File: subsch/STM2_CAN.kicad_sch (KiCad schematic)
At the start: 17 parts

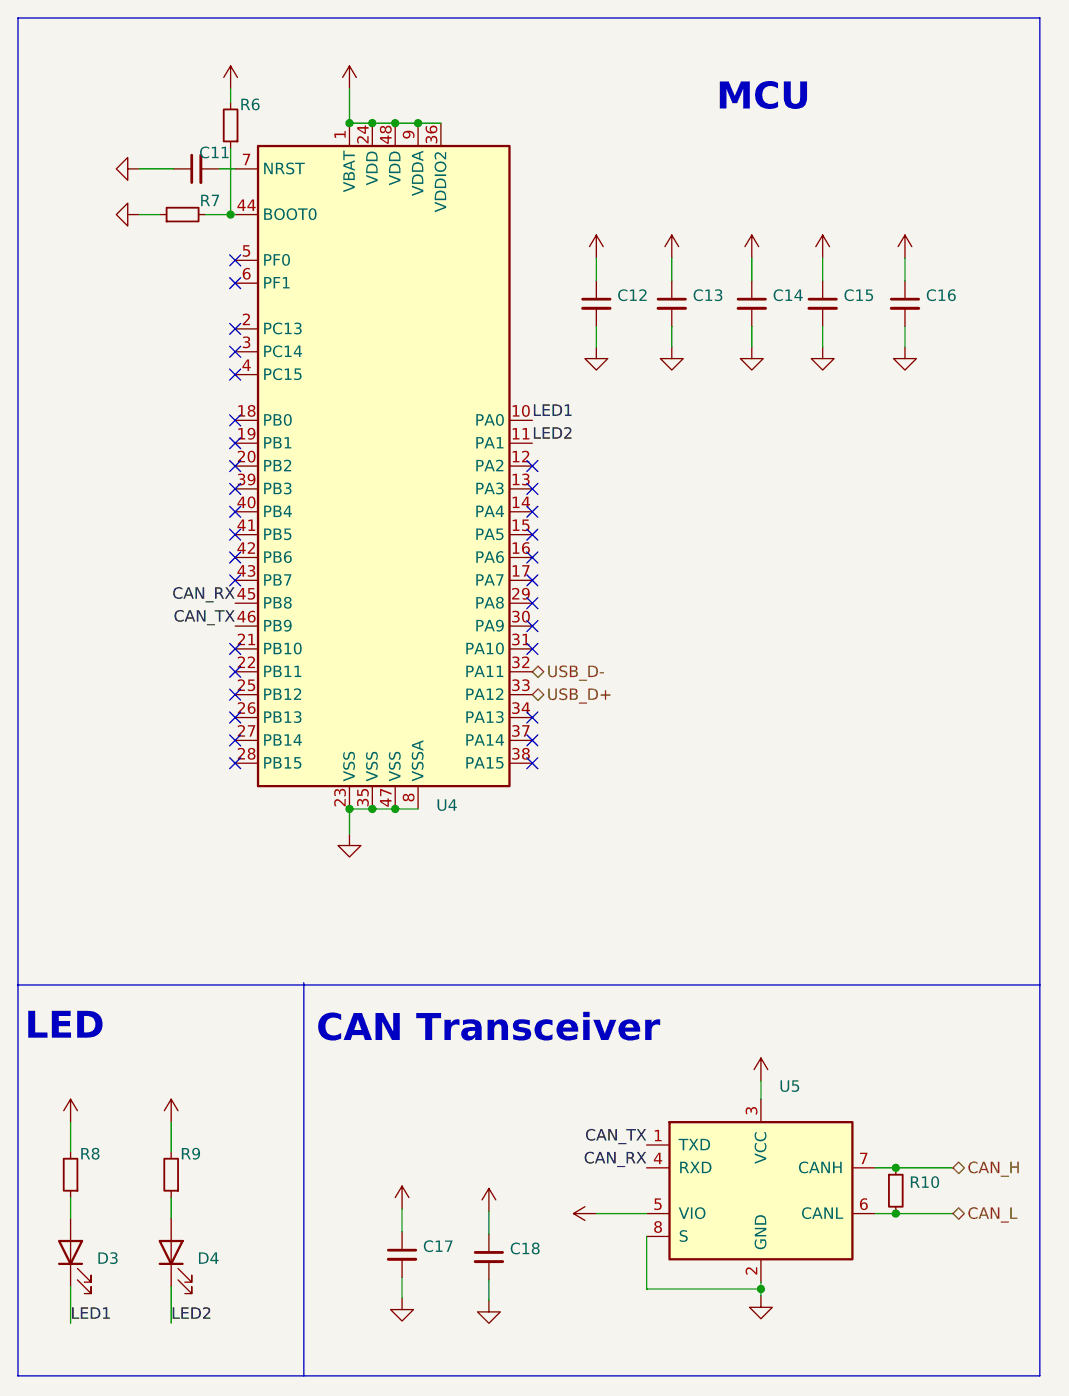
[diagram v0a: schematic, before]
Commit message: Big update on UART-pilot lamp/routings/connectors/esd protection
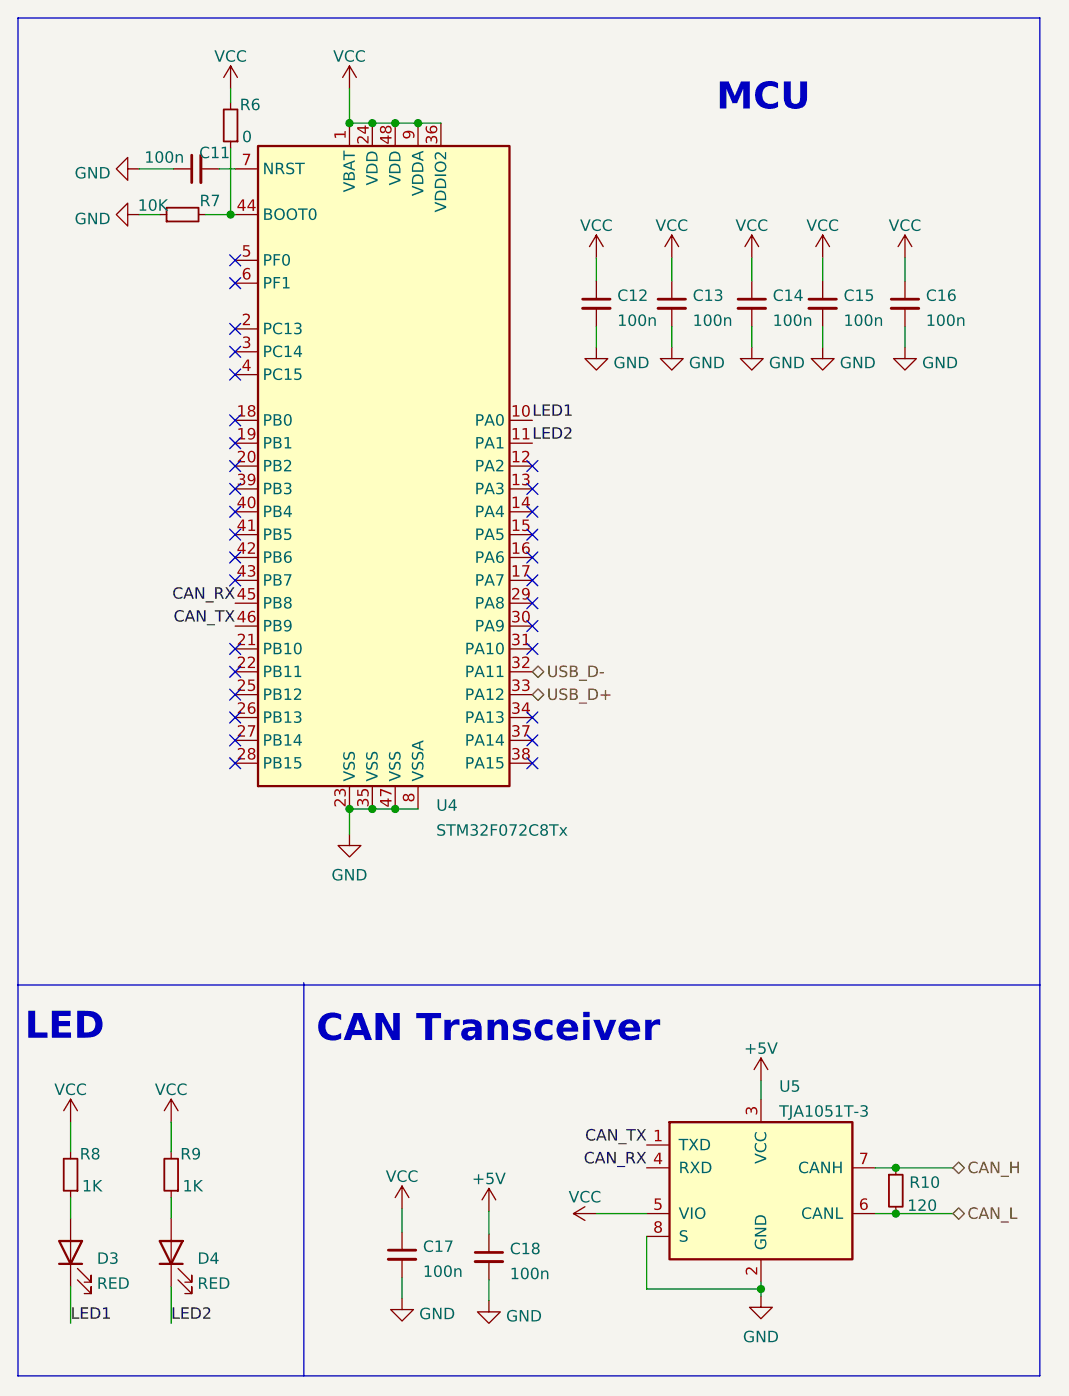
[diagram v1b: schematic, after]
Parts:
- C11, C12, C13, C14, C15, C16, C17, C18: value (none) -> 100n; footprint (none) -> Capacitor_SMD:C_0603_1608Metric
- D3, D4: value (none) -> RED; footprint (none) -> LED_SMD:LED_0603_1608Metric
- R10: value (none) -> 120; footprint (none) -> Resistor_SMD:R_0603_1608Metric
- R6: value (none) -> 0; footprint (none) -> Resistor_SMD:R_0603_1608Metric
- R7: value (none) -> 10K; footprint (none) -> Resistor_SMD:R_0603_1608Metric
- R8, R9: value (none) -> 1K; footprint (none) -> Resistor_SMD:R_0603_1608Metric
- U4: value (none) -> STM32F072C8Tx; footprint (none) -> Package_QFP:LQFP-48_7x7mm_P0.5mm
- U5: value (none) -> TJA1051T-3; footprint (none) -> Package_SO:SOIC-8_3.9x4.9mm_P1.27mm

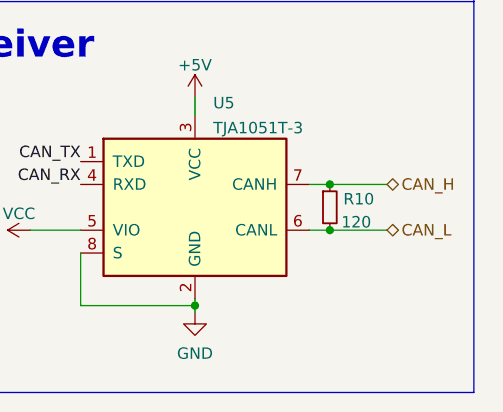
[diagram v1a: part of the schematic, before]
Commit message: Change connectors back to GH1.25&Add ESD for UART and CAN
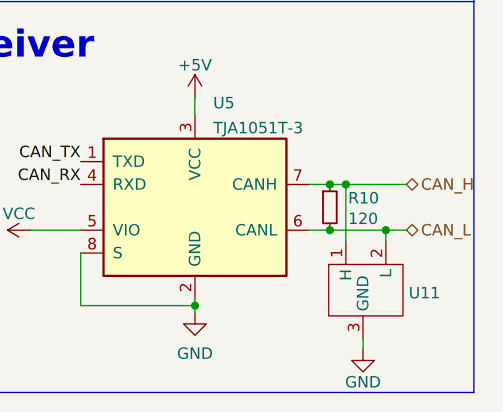
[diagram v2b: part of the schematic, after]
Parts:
- added U11: ~, Package_TO_SOT_SMD:SOT-23-3, symbol Extra IC:PESD1CAN
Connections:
- net CAN_H: now also U11.1 (H)
- net CAN_L: now also U11.2 (L)
- net GND: now also U11.3 (GND)
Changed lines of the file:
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@@
   (junction (at 134.366 160.782) (diameter 0) (color 0 0 0 0)
   )
+  (junction (at 136.144 160.782) (diameter 0) (color 0 0 0 0)
+  )
   (junction (at 119.38 174.244) (diameter 0) (color 0 0 0 0)
+  )
+  (junction (at 140.589 165.862) (diameter 0) (color 0 0 0 0)
   )
   (junction (at 134.366 165.862) (diameter 0) (color 0 0 0 0)
@@
     (stroke (width 0) (type default))
   )
+  (wire (pts (xy 134.366 160.782) (xy 136.144 160.782))
+    (stroke (width 0) (type default))
+  )
   (wire (pts (xy 76.2 44.704) (xy 78.74 44.704))
     (stroke (width 0) (type default))
@@
     (stroke (width 0) (type default))
   )
+  (wire (pts (xy 136.144 160.782) (xy 142.875 160.782))
+    (stroke (width 0) (type default))
+  )
   (polyline (pts (xy 150.368 183.896) (xy 150.368 140.462))
     (stroke (width 0) (type default))
@@
     (stroke (width 0) (type default))
   )
+  (wire (pts (xy 136.144 160.782) (xy 136.144 167.132))
+    (stroke (width 0) (type default))
+  )
   (wire (pts (xy 50.292 49.784) (xy 54.102 49.784))
     (stroke (width 0) (type default))
@@
     (stroke (width 0) (type default))
   )
-  (wire (pts (xy 134.366 165.862) (xy 140.716 165.862))
-    (stroke (width 0) (type default))
-  )
-  (wire (pts (xy 134.366 160.782) (xy 140.716 160.782))
-    (stroke (width 0) (type default))
-  )
   (wire (pts (xy 42.672 164.084) (xy 42.672 166.37))
     (stroke (width 0) (type default))
@@
     (stroke (width 0) (type default))
   )
+  (wire (pts (xy 138.049 179.07) (xy 138.049 177.927))
+    (stroke (width 0) (type default))
+  )
   (wire (pts (xy 109.474 67.31) (xy 109.474 69.596))
     (stroke (width 0) (type default))
@@
     (stroke (width 0) (type default))
   )
+  (wire (pts (xy 134.366 165.862) (xy 140.589 165.862))
+    (stroke (width 0) (type default))
+  )
   (wire (pts (xy 60.452 54.864) (xy 60.96 54.864))
     (stroke (width 0) (type default))
@@
     (stroke (width 0) (type default))
   )
+  (wire (pts (xy 140.589 165.862) (xy 142.875 165.862))
+    (stroke (width 0) (type default))
+  )
   (wire (pts (xy 76.2 120.904) (xy 78.74 120.904))
+    (stroke (width 0) (type default))
+  )
+  (wire (pts (xy 140.589 165.862) (xy 140.589 167.132))
     (stroke (width 0) (type default))
   )
@@
     (effects (font (size 1.27 1.27)) (justify right bottom))
   )
-  (hierarchical_label "CAN_L" (shape bidirectional) (at 140.716 165.862 0) (fields_autoplaced)
+  (hierarchical_label "CAN_L" (shape bidirectional) (at 142.875 165.862 0) (fields_autoplaced)
     (effects (font (size 1.27 1.27)) (justify left))
   )
@@
     (effects (font (size 1.27 1.27)) (justify left))
   )
-  (hierarchical_label "CAN_H" (shape bidirectional) (at 140.716 160.782 0) (fields_autoplaced)
+  (hierarchical_label "CAN_H" (shape bidirectional) (at 142.875 160.782 0) (fields_autoplaced)
     (effects (font (size 1.27 1.27)) (justify left))
   )
@@
         (path "/e63e39d7-6ac0-4ffd-8aa3-1841a4541b55/9b90d3c5-a48b-42a5-8d7c-de34d4b66dbc"
           (reference "#PWR041") (unit 1)
+        )
+      )
+    )
+  )
+  (symbol (lib_id "Extra IC:PESD1CAN") (at 138.684 173.482 0) (unit 1)
+    (in_bom yes) (on_board yes) (dnp no) (fields_autoplaced)
+    (property "Reference" "U11" (at 143.129 172.8463 0)
+      (effects (font (size 1.27 1.27)) (justify left))
+    )
+    (property "Value" "~" (at 137.414 167.132 0)
+      (effects (font (size 1.27 1.27)))
+    )
+    (property "Footprint" "Package_TO_SOT_SMD:SOT-23-3" (at 137.414 167.132 0)
+      (effects (font (size 1.27 1.27)) hide)
+    )
+    (property "Datasheet" "" (at 137.414 167.132 0)
+      (effects (font (size 1.27 1.27)) hide)
+    )
+    (pin "1")
+    (pin "2")
+    (pin "3")
+    (instances
+      (project "USB2XXX"
+        (path "/e63e39d7-6ac0-4ffd-8aa3-1841a4541b55/9b90d3c5-a48b-42a5-8d7c-de34d4b66dbc"
+          (reference "U11") (unit 1)
         )
       )
@@
   (symbol (lib_id "Device:R_Small") (at 134.366 163.322 0) (unit 1)
     (in_bom yes) (on_board yes) (dnp no)
-    (property "Reference" "R10" (at 135.8646 162.4135 0)
-      (effects (font (size 1.27 1.27)) (justify left))
-    )
-    (property "Value" "120" (at 135.636 164.973 0)
+    (property "Reference" "R10" (at 136.398 162.306 0)
+      (effects (font (size 1.27 1.27)) (justify left))
+    )
+    (property "Value" "120" (at 136.398 164.592 0)
       (effects (font (size 1.27 1.27)) (justify left))
     )
@@
         )
       )
+    )
+  )
+  (symbol (lib_id "power:GND") (at 138.049 179.07 0) (unit 1)
+    (in_bom yes) (on_board yes) (dnp no)
+    (property "Reference" "#PWR022" (at 138.049 185.42 0)
+      (effects (font (size 1.27 1.27)) hide)
+    )
+    (property "Value" "GND" (at 138.049 182.753 0)
+      (effects (font (size 1.27 1.27)))
+    )
+    (property "Footprint" "" (at 138.049 179.07 0)
+      (effects (font (size 1.27 1.27)) hide)
+    )
+    (property "Datasheet" "" (at 138.049 179.07 0)
+      (effects (font (size 1.27 1.27)) hide)
+    )
+    (pin "1")
+    (instances
+      (project "USB2XXX"
+        (path "/e63e39d7-6ac0-4ffd-8aa3-1841a4541b55/863ee6bd-9a8e-49fb-84d6-8d00fe76baf1"
+          (reference "#PWR022") (unit 1)
+        )
+        (path "/e63e39d7-6ac0-4ffd-8aa3-1841a4541b55/9b90d3c5-a48b-42a5-8d7c-de34d4b66dbc"
+          (reference "#PWR086") (unit 1)
+        )
+      )

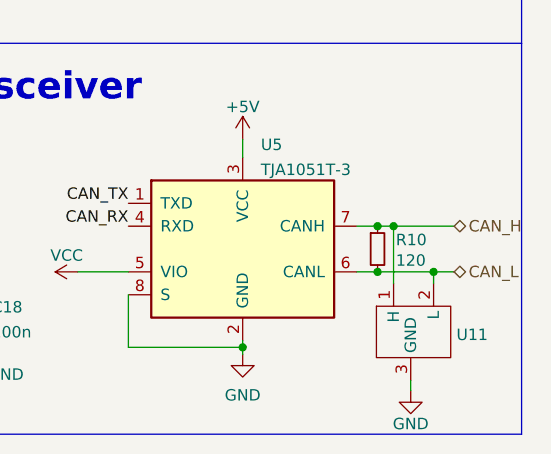
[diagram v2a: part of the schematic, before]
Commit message: Adaption for SMT(hotfix)
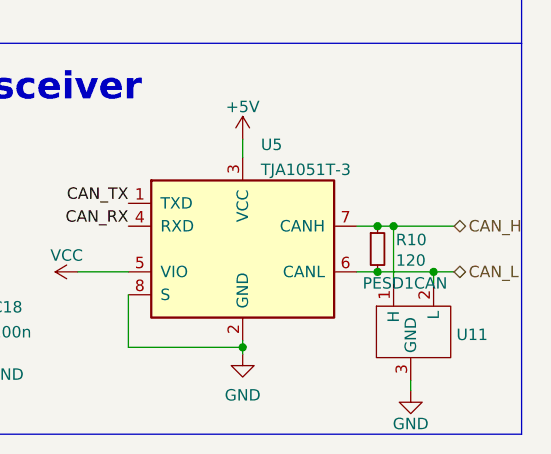
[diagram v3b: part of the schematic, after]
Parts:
- U11: value ~ -> PESD1CAN
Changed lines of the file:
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@@
       (effects (font (size 1.27 1.27)) (justify left))
     )
-    (property "Value" "~" (at 137.414 167.132 0)
+    (property "Value" "PESD1CAN" (at 137.414 167.132 0)
       (effects (font (size 1.27 1.27)))
     )
